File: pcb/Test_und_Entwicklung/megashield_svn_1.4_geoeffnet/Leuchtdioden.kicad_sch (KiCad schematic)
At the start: 47 parts, among them IC1 UDN 2987 LWTR-6T, P10 Status LEDs GND, P50 Led Panel, P7 Status LEDs, Q14 BC817, Q15 BC817, Q16 BC817, Q17 BC817, Q18 BC817, Q19 BC817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

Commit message: megashield_svn_1.4_geoeffnet
megashield_svn_1.4_geoeffnet
32 Q3,Q12-Q23,Q1,Q38 neue JLCPCB Nummer
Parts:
- Q14, Q15, Q16, Q17, Q18, Q19, Q20, Q21, Q22, Q23: Gehäuseart (none) -> SOT-23
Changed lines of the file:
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@@
+      (effects (font (size 1.27 1.27)) hide)
+    )
+    (property "Gehäuseart" "SOT-23" (id 7) (at 34.29 53.848 0)
       (effects (font (size 1.27 1.27)) hide)
     )
@@
       (effects (font (size 1.27 1.27)) hide)
     )
+    (property "Gehäuseart" "SOT-23" (id 7) (at 40.894 40.132 0)
+      (effects (font (size 1.27 1.27)) hide)
+    )
   )
   (symbol (lib_id "ardumower-mega-shield-svn-rescue:BC817-40-RESCUE-ardumower_mega_shield_svn") (at 101.727 54.356 0) (mirror y) (unit 1)
@@
       (effects (font (size 1.27 1.27)) hide)
     )
+    (property "Gehäuseart" "SOT-23" (id 7) (at 101.727 54.356 0)
+      (effects (font (size 1.27 1.27)) hide)
+    )
   )
   (symbol (lib_id "ardumower-mega-shield-svn-rescue:BC817-40-RESCUE-ardumower_mega_shield_svn") (at 108.331 40.64 0) (unit 1)
@@
       (effects (font (size 1.27 1.27)) hide)
     )
+    (property "Gehäuseart" "SOT-23" (id 7) (at 108.331 40.64 0)
+      (effects (font (size 1.27 1.27)) hide)
+    )
   )
   (symbol (lib_id "ardumower-mega-shield-svn-rescue:BC817-40-RESCUE-ardumower_mega_shield_svn") (at 172.72 54.864 0) (mirror y) (unit 1)
@@
       (effects (font (size 1.27 1.27)) hide)
     )
+    (property "Gehäuseart" "SOT-23" (id 7) (at 172.72 54.864 0)
+      (effects (font (size 1.27 1.27)) hide)
+    )
   )
   (symbol (lib_id "ardumower-mega-shield-svn-rescue:BC817-40-RESCUE-ardumower_mega_shield_svn") (at 179.324 41.148 0) (unit 1)
@@
       (effects (font (size 1.27 1.27)) hide)
     )
+    (property "Gehäuseart" "SOT-23" (id 7) (at 179.324 41.148 0)
+      (effects (font (size 1.27 1.27)) hide)
+    )
   )
   (symbol (lib_id "ardumower-mega-shield-svn-rescue:BC817-40-RESCUE-ardumower_mega_shield_svn") (at 221.234 115.697 0) (mirror y) (unit 1)
@@
       (effects (font (size 1.27 1.27)) hide)
     )
+    (property "Gehäuseart" "SOT-23" (id 7) (at 221.234 115.697 0)
+      (effects (font (size 1.27 1.27)) hide)
+    )
   )
   (symbol (lib_id "ardumower-mega-shield-svn-rescue:BC817-40-RESCUE-ardumower_mega_shield_svn") (at 227.838 129.413 0) (unit 1)
@@
       (effects (font (size 1.27 1.27)) hide)
     )
+    (property "Gehäuseart" "SOT-23" (id 7) (at 227.838 129.413 0)
+      (effects (font (size 1.27 1.27)) hide)
+    )
   )
   (symbol (lib_id "ardumower-mega-shield-svn-rescue:BC817-40-RESCUE-ardumower_mega_shield_svn") (at 256.54 116.078 0) (mirror y) (unit 1)
@@
       (effects (font (size 1.27 1.27)) hide)
     )
+    (property "Gehäuseart" "SOT-23" (id 7) (at 256.54 116.078 0)
+      (effects (font (size 1.27 1.27)) hide)
+    )
   )
   (symbol (lib_id "ardumower-mega-shield-svn-rescue:BC817-40-RESCUE-ardumower_mega_shield_svn") (at 263.144 129.794 0) (unit 1)
@@
       (effects (font (size 1.27 1.27)) hide)
     )
+    (property "Gehäuseart" "SOT-23" (id 7) (at 263.144 129.794 0)
+      (effects (font (size 1.27 1.27)) hide)
+    )

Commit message: megashield_svn_1.4_geoeffnet
megashield_svn_1.4_geoeffnet
40 D17-23 Footprint auf 0805 umgeändert  + neue JLCPCB Nummer
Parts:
- D17: footprint LEDs:LED_1206 -> LED_SMD:LED_0805_2012Metric; Bestelllink https://www.reichelt.de/de/en/green-smd-led-with-dome-lens-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 -> (none); Bestellnummer R: SMD-LED 1206K GN -> (none); Funktion Green SMD LED with dome lens, 200 mcd -> (none); Gehäuseart 3216 (1206) -> 0805; JLCPCB Basic / Extern 1 -> (none); Reichelt-Bestellnummer R: SMD-LED 1206K GN -> (none); Technische Daten Green SMD LED with dome lens, 200 mcd -> Green SMD LED
- D18, D19, D20, D21, D22, D23: footprint LEDs:LED_1206 -> LED_SMD:LED_0805_2012Metric; Bestelllink https://www.reichelt.de/de/en/green-smd-led-with-dome-lens-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 -> (none); Gehäuseart 3216 (1206) -> 0805; JLCPCB Basic / Extern 1 -> (none); Reichelt-Bestellnummer R: SMD-LED 1206K GN -> (none)

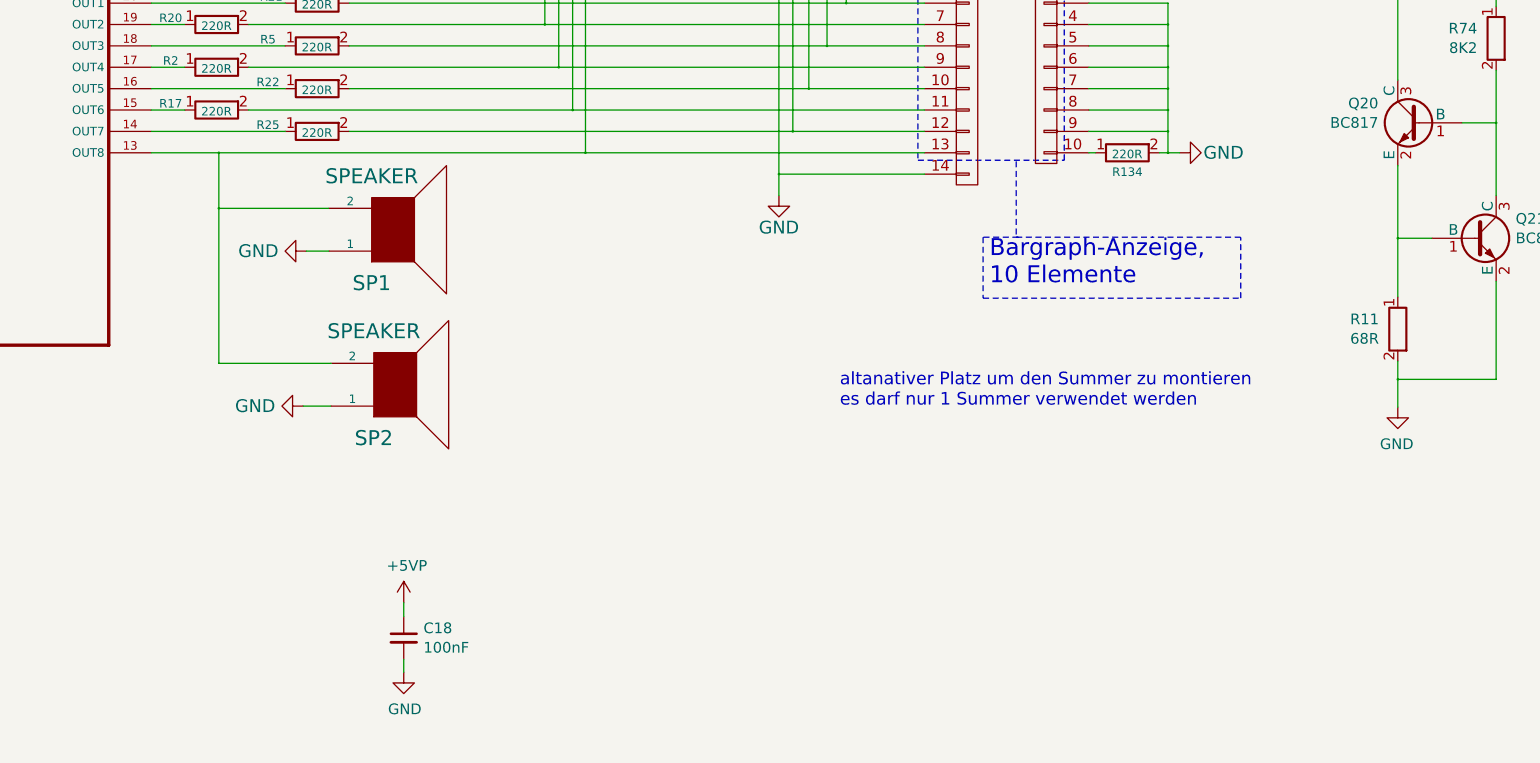
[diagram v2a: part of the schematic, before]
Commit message: megashield_svn_1.4_geoeffnet
megashield_svn_1.4_geoeffnet
41 Q24 + R6 hinzugefügt und Summer ansteuerung umgeändert
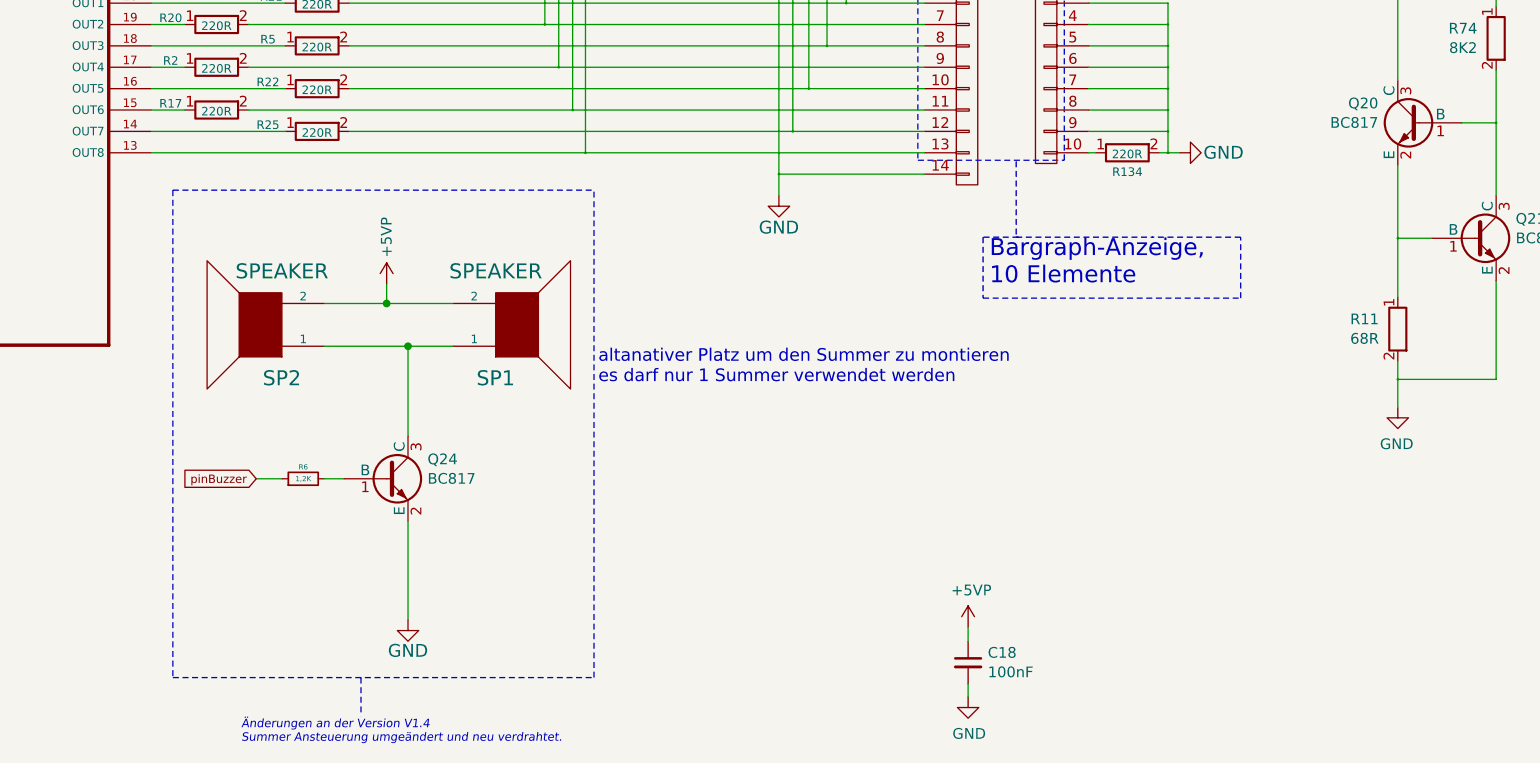
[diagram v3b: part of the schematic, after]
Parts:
- added Q24: BC817, Package_TO_SOT_SMD:SOT-23, symbol ardumower-mega-shield-svn-rescue:BC817-40-RESCUE-ardumower_mega_shield_svn
- added R6: 1,2K, Resistor_SMD:R_0603_1608Metric, symbol ardumower-mega-shield-svn-rescue:R_Small-RESCUE-ardumower_mega_shield_svn
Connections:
- net +5VP: now also SP1.2, SP2.2
- net GND: now also Q24.2 (E); no longer SP1.1, SP2.1
- net pinBuzzer: now also R6.1
- net at IC1.13 (OUT8), P50.13 (P13), P7.13 (P13): no longer SP1.2, SP2.2
- new net: Q24.3 (C), SP1.1, SP2.1
- new net: Q24.1 (B), R6.2
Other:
- note added: "Änderungen an der Version V1.4 Summer Ansteuerung umgeändert und neu verdrahtet."
- company: ML AG JL UZ -> ML AG JL BS UZ
- moved on the sheet: C18, SP1, SP2

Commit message: megashield_svn_1.4_geoeffnet
megashield_svn_1.4_geoeffnet
42 IC1 Bestückung deaktiviert und Symbol in 3D Ansicht deakteviert
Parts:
- IC1: Bestücken (Assemble) JA (YES) -> NEIN (NO)

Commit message: megashield_svn_1.4_geoeffnet
megashield_svn_1.4_geoeffnet
45  R1,R2,R5,R17,R20,R21,R22,R25,R77,R134 Footprint geändert und JLCPCB Nummer geändert
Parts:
- D17, D18, D19, D20, D21, D22, D23: JLCPCB LCSC Part C375460 -> C2296
- R1, R134, R17, R2, R20, R21, R22, R25, R5, R77: footprint Zimprich:R_1206 -> Resistor_SMD:R_0805_2012Metric; Bauform (none) -> 0805; Bestelllink https://www.reichelt.de/de/en/smd-resistor-1206-220-ohm-125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 -> https://www.reichelt.de/de/en/smd-resistor-0805-220-ohm-100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; Bestellnummer R: RND 1206 1 220 -> R: RND 0805 1 220; Funktion SMD Resistor 1206, 220 Ohm, 125 mW, 1% -> SMD Resistor 0805, 220 Ohm, 100 mW, 1%; Gehäuseart 1206 -> 0805; JLCPCB LCSC Part C17957 -> C17557; Reichelt-Bestellnummer R: RND 1206 1 220 -> R: RND 0805 1 220; Technische Daten SMD Resistor 1206, 220 Ohm, 125 mW, 1% -> SMD Resistor 0805, 220 Ohm, 100 mW, 1%

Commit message: megashield_svn_1.4_geoeffnet
megashield_svn_1.4_geoeffnet
47 R36 & R11,R73,R79 Footprint und JLCPCB Nummer geändert
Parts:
- R11, R79: footprint Zimprich:R_1206 -> Resistor_SMD:R_0805_2012Metric; Bauform (none) -> 0805; Bestelllink https://www.reichelt.de/de/en/smd-resistor-1206-68-ohm-125-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 -> https://www.reichelt.de/de/en/smd-resistor-0805-68-ohm-100-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; Bestellnummer R: RND 1206 1 68 -> R: RND 0805 1 68; Funktion SMD Resistor 1206, 68 Ohm, 125 mW, 1% -> SMD Resistor 0805, 68 Ohm, 100 mW, 1%; Gehäuseart 1206 -> 0805; JLCPCB LCSC Part C17976 -> C17802; Reichelt-Bestellnummer R: RND 1206 1 68 -> R: RND 0805 1 68; Technische Daten SMD Resistor 1206, 68 Ohm, 125 mW, 1% -> SMD Resistor 0805, 68 Ohm, 100 mW, 1%
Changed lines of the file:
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@@
   (title_block
     (title "Ardumower shield SVN Version")
-    (date "2021-01-14")
+    (date "2021-01-15")
     (rev "1.4")
     (company "ML AG JL BS UZ")
@@
       (effects (font (size 1.27 1.27)) (justify left))
     )
-    (property "Footprint" "Zimprich:R_1206" (id 2) (at 220.472 140.208 90)
+    (property "Footprint" "Resistor_SMD:R_0805_2012Metric" (id 2) (at 220.472 140.208 90)
       (effects (font (size 1.27 1.27)) hide)
     )
-    (property "Datasheet" "" (id 3) (at 218.694 140.208 0)
+    (property "Datasheet" "https://cdn-reichelt.de/documents/datenblatt/B300/RND_SMD_0805_RESISTOR_2017.pdf" (id 3) (at 218.694 140.208 0)
       (effects (font (size 1.27 1.27)) hide)
     )
-    (property "Gehäuseart" "1206" (id 4) (at 218.694 140.208 0)
+    (property "Gehäuseart" "0805" (id 4) (at 218.694 140.208 0)
       (effects (font (size 1.524 1.524)) hide)
     )
-    (property "Bestelllink" "https://www.reichelt.de/de/en/smd-resistor-1206-68-ohm-125-mw-1--rnd-1206-1-68-p183346.html?GROUPID=7973&SEARCH=rnd%2B1206%2B1%2B68%252C0&&r=1" (id 5) (at 218.694 140.208 0)
+    (property "Bestelllink" "https://www.reichelt.de/de/en/smd-resistor-0805-68-ohm-100-mw-1--rnd-0805-1-68-p183168.html?search=RND+0805+1+68&&r=1" (id 5) (at 218.694 140.208 0)
       (effects (font (size 1.524 1.524)) hide)
     )
-    (property "Technische Daten" "SMD Resistor 1206, 68 Ohm, 125 mW, 1%" (id 6) (at 218.694 140.208 0)
+    (property "Technische Daten" "SMD Resistor 0805, 68 Ohm, 100 mW, 1%" (id 6) (at 218.694 140.208 0)
       (effects (font (size 1.524 1.524)) hide)
     )
-    (property "Bestellnummer" "R: RND 1206 1 68" (id 7) (at 218.694 140.208 0)
+    (property "Bestellnummer" "R: RND 0805 1 68" (id 7) (at 218.694 140.208 0)
       (effects (font (size 1.524 1.524)) hide)
     )
-    (property "Bauform" "" (id 8) (at 218.694 140.208 0)
+    (property "Bauform" "0805" (id 8) (at 218.694 140.208 0)
       (effects (font (size 1.524 1.524)) hide)
     )
-    (property "Funktion" "SMD Resistor 1206, 68 Ohm, 125 mW, 1%" (id 9) (at 218.694 140.208 0)
+    (property "Funktion" "SMD Resistor 0805, 68 Ohm, 100 mW, 1%" (id 9) (at 218.694 140.208 0)
       (effects (font (size 1.524 1.524)) hide)
     )
@@
       (effects (font (size 1.27 1.27)) hide)
     )
-    (property "Reichelt-Bestellnummer" "R: RND 1206 1 68" (id 5) (at 218.694 140.208 0)
+    (property "Reichelt-Bestellnummer" "R: RND 0805 1 68" (id 5) (at 218.694 140.208 0)
       (effects (font (size 1.27 1.27)) hide)
     )
-    (property "JLCPCB LCSC Part" "C17976" (id 6) (at 218.694 140.208 0)
+    (property "JLCPCB LCSC Part" "C17802" (id 6) (at 218.694 140.208 0)
       (effects (font (size 1.27 1.27)) hide)
     )
@@
       (effects (font (size 1.27 1.27)) (justify left))
     )
-    (property "Footprint" "Zimprich:R_1206" (id 2) (at 255.778 140.589 90)
+    (property "Footprint" "Resistor_SMD:R_0805_2012Metric" (id 2) (at 255.778 140.589 90)
       (effects (font (size 1.27 1.27)) hide)
     )
-    (property "Datasheet" "" (id 3) (at 254 140.589 0)
+    (property "Datasheet" "https://cdn-reichelt.de/documents/datenblatt/B300/RND_SMD_0805_RESISTOR_2017.pdf" (id 3) (at 254 140.589 0)
       (effects (font (size 1.27 1.27)) hide)
     )
-    (property "Gehäuseart" "1206" (id 4) (at 254 140.589 0)
+    (property "Gehäuseart" "0805" (id 4) (at 254 140.589 0)
       (effects (font (size 1.524 1.524)) hide)
     )
-    (property "Bestelllink" "https://www.reichelt.de/de/en/smd-resistor-1206-68-ohm-125-mw-1--rnd-1206-1-68-p183346.html?GROUPID=7973&SEARCH=rnd%2B1206%2B1%2B68%252C0&&r=1" (id 5) (at 254 140.589 0)
+    (property "Bestelllink" "https://www.reichelt.de/de/en/smd-resistor-0805-68-ohm-100-mw-1--rnd-0805-1-68-p183168.html?search=RND+0805+1+68&&r=1" (id 5) (at 254 140.589 0)
       (effects (font (size 1.524 1.524)) hide)
     )
-    (property "Technische Daten" "SMD Resistor 1206, 68 Ohm, 125 mW, 1%" (id 6) (at 254 140.589 0)
+    (property "Technische Daten" "SMD Resistor 0805, 68 Ohm, 100 mW, 1%" (id 6) (at 254 140.589 0)
       (effects (font (size 1.524 1.524)) hide)
     )
-    (property "Bestellnummer" "R: RND 1206 1 68" (id 7) (at 254 140.589 0)
+    (property "Bestellnummer" "R: RND 0805 1 68" (id 7) (at 254 140.589 0)
       (effects (font (size 1.524 1.524)) hide)
     )
-    (property "Bauform" "" (id 8) (at 254 140.589 0)
+    (property "Bauform" "0805" (id 8) (at 254 140.589 0)
       (effects (font (size 1.524 1.524)) hide)
     )
-    (property "Funktion" "SMD Resistor 1206, 68 Ohm, 125 mW, 1%" (id 9) (at 254 140.589 0)
+    (property "Funktion" "SMD Resistor 0805, 68 Ohm, 100 mW, 1%" (id 9) (at 254 140.589 0)
       (effects (font (size 1.524 1.524)) hide)
     )
@@
       (effects (font (size 1.27 1.27)) hide)
     )
-    (property "Reichelt-Bestellnummer" "R: RND 1206 1 68" (id 5) (at 254 140.589 0)
+    (property "Reichelt-Bestellnummer" "R: RND 0805 1 68" (id 5) (at 254 140.589 0)
       (effects (font (size 1.27 1.27)) hide)
     )
-    (property "JLCPCB LCSC Part" "C17976" (id 6) (at 254 140.589 0)
+    (property "JLCPCB LCSC Part" "C17802" (id 6) (at 254 140.589 0)
       (effects (font (size 1.27 1.27)) hide)
     )
